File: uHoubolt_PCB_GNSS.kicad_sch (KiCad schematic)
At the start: 104 parts, among them J1 Power In, J10 CAN1, J11 CAN2, J12 MMCX-J-P-H-ST-SM1, J2 Debug, J3 Debug, J4 CAN1, J5 CAN2, J6 CAN1, J7 CAN2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

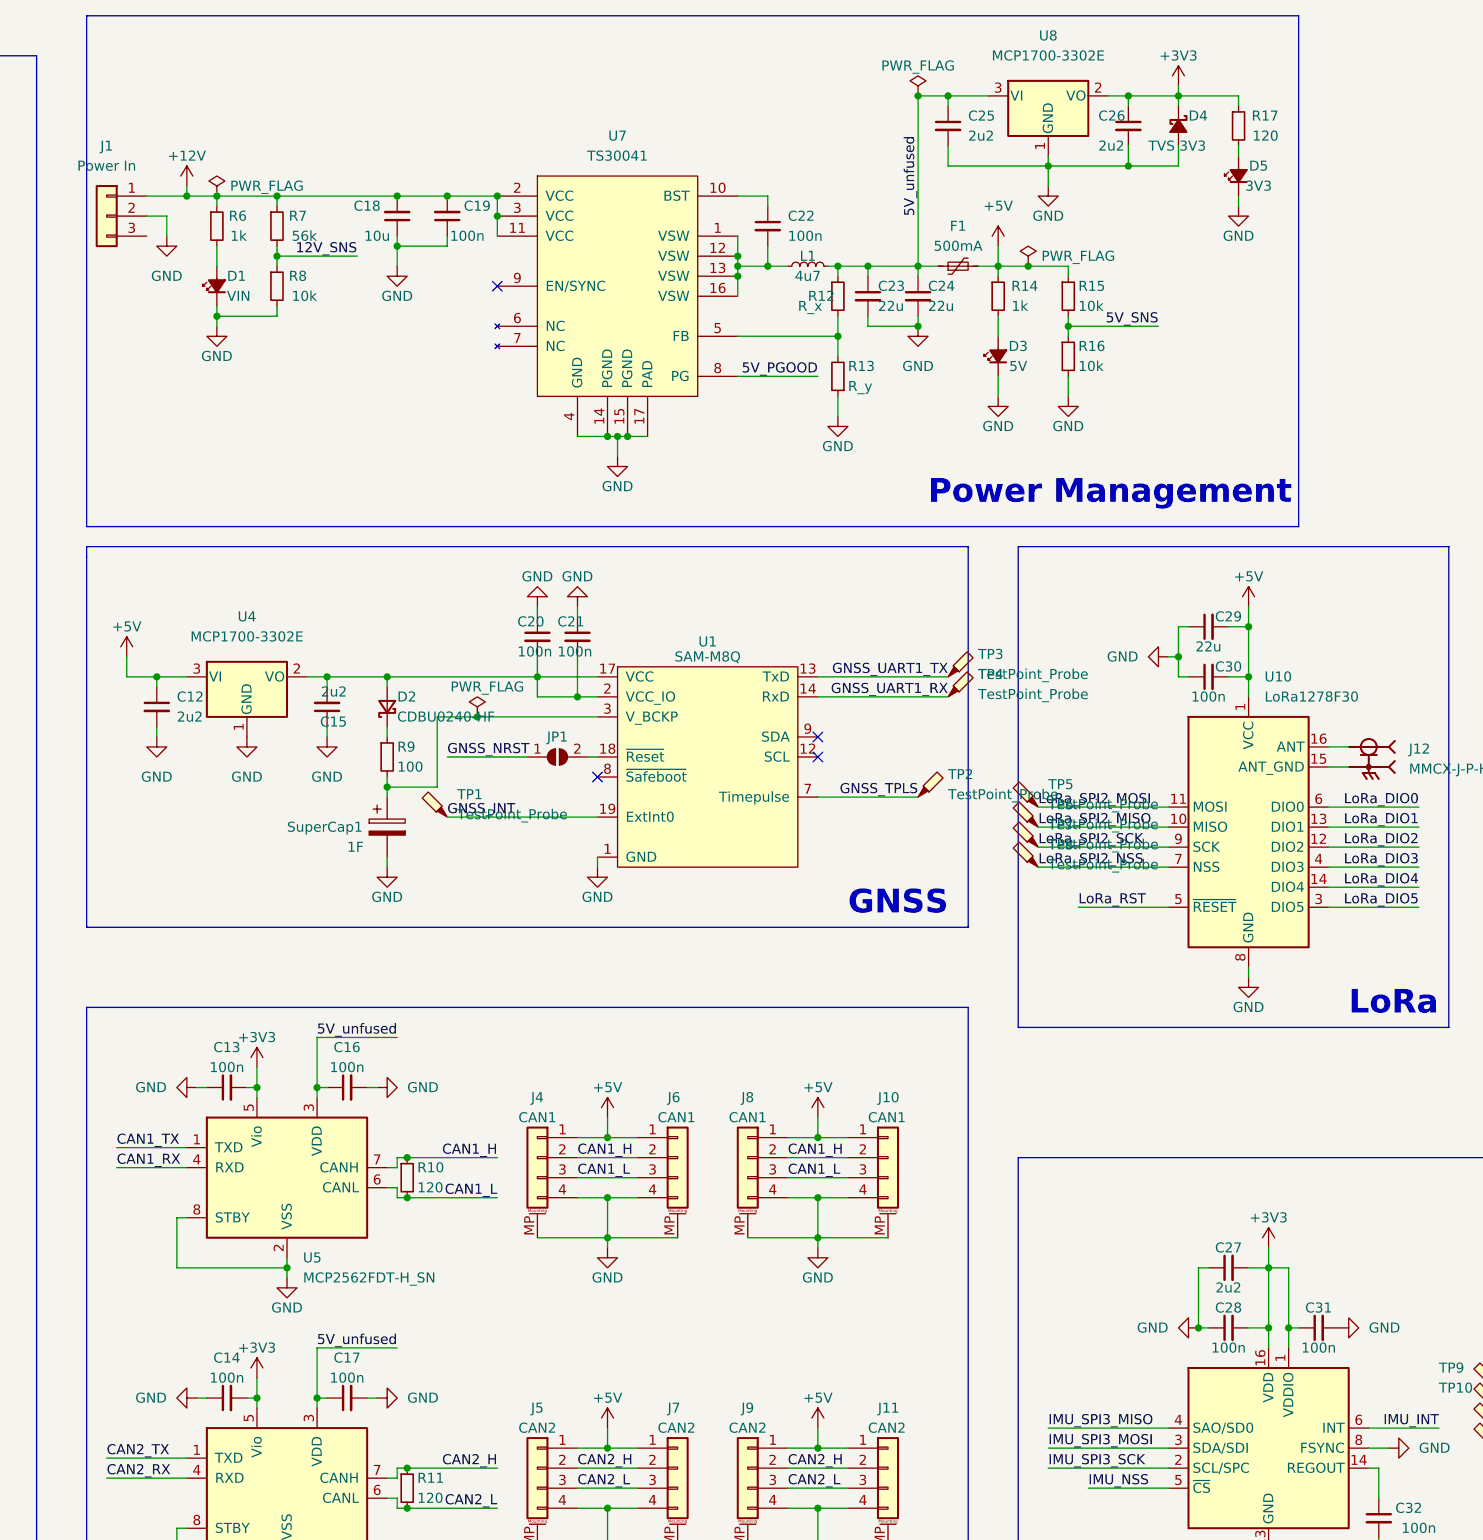
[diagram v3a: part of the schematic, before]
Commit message: Updated layout; global placement done
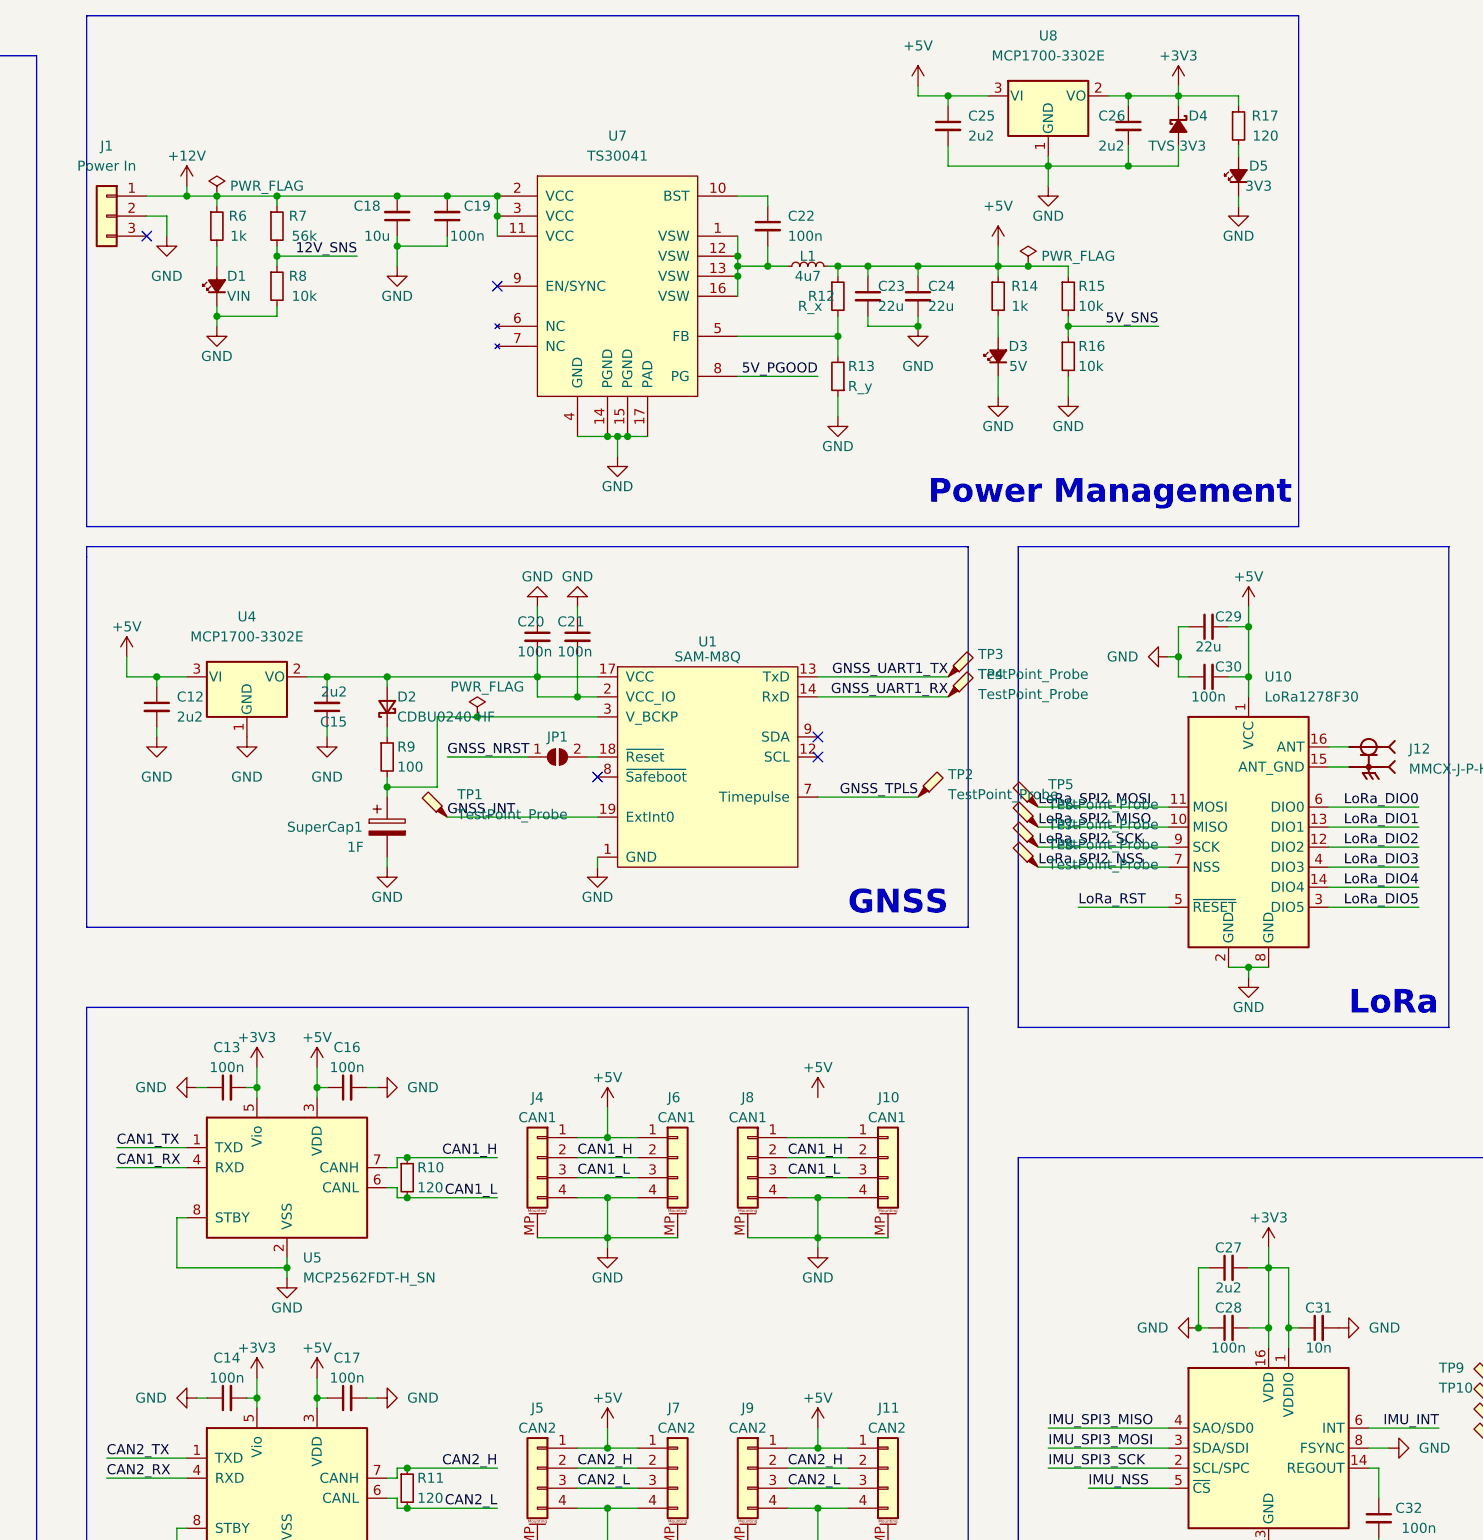
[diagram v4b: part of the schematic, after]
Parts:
- removed F1: 500mA, Fuse:Fuse_0603_1608Metric, symbol Device:Polyfuse_Small
- C31: value 100n -> 10n
- D1, D3, D5: footprint LED_SMD:LED_0201_0603Metric -> LED_SMD:LED_0603_1608Metric
- U10: footprint (none) -> TXV_Library_Footprints:G-NiceRF-LoRa1278F30
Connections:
- net 5V_unfused is gone; now on net +5V: C16.1, C17.1, C23.1, C24.1, C25.1, L1.2, R12.1, U5.3 (VDD), U6.3 (VDD), U8.3 (VI)
- net +5V: no longer J10.1 (Pin_1), J8.1 (Pin_1)
- net GND: now also U10.2 (GND)
- new net: J10.1 (Pin_1), J8.1 (Pin_1)
- no-connect marks 27 -> 28

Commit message: Update layout further
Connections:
- net +5V: now also J10.1 (Pin_1), J8.1 (Pin_1)
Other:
- moved on the sheet: C29, C30, C33, C34, J12, TP10, TP11, TP12, TP5, TP6, TP7, TP8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

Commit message: Finished 1st proper layout
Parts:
- removed TP1, TP10, TP11, TP12, TP2, TP3, TP4, TP5, TP6, TP7, TP8, TP9: TestPoint_Probe, TestPoint:TestPoint_Pad_D1.0mm, symbol Connector:TestPoint_Probe

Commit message: Update CAN transceiver footprints; removed redundant CAN jacks; replaced Power In Conn
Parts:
- removed J1: Power In, TXV_Library_Footprints:Molex_MegaFit_1x03_Vertical, symbol Connector_Generic:Conn_01x03
- removed J10, J8: CAN1, Connector_JST:JST_GH_BM04B-GHS-TBT_1x04-1MP_P1.25mm_Vertical, symbol Connector_Generic_MountingPin:Conn_01x04_MountingPin
- removed J11, J9: CAN2, Connector_JST:JST_GH_BM04B-GHS-TBT_1x04-1MP_P1.25mm_Vertical, symbol Connector_Generic_MountingPin:Conn_01x04_MountingPin
- removed J12: MMCX-J-P-H-ST-SM1, TXV_Library_Footprints:SAMTEC_MMCX-J-P-H-ST-SM1, symbol add_components:MMCX-J-P-H-ST-SM1
- removed U5, U6: MCP2562FDT-H_SN, Package_SO:SOIC-8_3.9x4.9mm_P1.27mm, symbol TXV_Library_Symbols:MCP2562FDT-H_SN
- added C35: 100n, Capacitor_SMD:C_0603_1608Metric, symbol Device:C_Small
- added J1: Power In, TXV_Library_Footprints:Molex_Nano-Fit_105309-xx02_1x02_P2.50mm_Vertical, symbol Connector_Generic:Conn_01x02
- added J12: MMCX-J-P-H-RA-SM1, SAMTEC_MMCX-J-P-H-RA-SM1, symbol TXV_Library_Symbols:MMCX-J-P-H-RA-SM1
- added U5, U6: MCP2562FDT, Package_DFN_QFN:DFN-8-1EP_3x3mm_P0.65mm_EP1.55x2.4mm, symbol TXV_Library_Symbols:MCP2562FDT
- C18, C29: footprint Capacitor_SMD:C_0603_1608Metric -> Capacitor_SMD:C_0805_2012Metric
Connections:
- net +12V: now also J1.1 (Pin_1)
- net +3V3: now also U5.5 (Vio), U6.5 (Vio)
- net +5V: now also U5.3 (VDD), U6.3 (VDD)
- net CAN1_H: now also U5.7 (CANH)
- net CAN1_L: now also U5.6 (CANL)
- net CAN1_RX: now also U5.4 (RXD)
- net CAN1_TX: now also U5.1 (TXD)
- net CAN2_H: now also U6.7 (CANH)
- net CAN2_L: now also U6.6 (CANL)
- net CAN2_RX: now also U6.4 (RXD)
- net CAN2_TX: now also U6.1 (TXD)
- net GND: now also C35.2, J1.2 (Pin_2), U5.2 (VSS), U5.8 (STBY), U5.9 (PAD), U6.2 (VSS), U6.8 (STBY), U6.9 (PAD)
- net NRST: now also R1.2, U2.7 (PG10-NRST), C35.1
- net SWCLK: now also U2.64 (PA14)
- net SWDIO: now also U2.63 (PA13)
- net at U10.15 (ANT_GND): now also J12.S1, J12.S2, J12.S3, J12.S4
- net at U10.16 (ANT): now also J12.1
- no-connect marks 28 -> 25
